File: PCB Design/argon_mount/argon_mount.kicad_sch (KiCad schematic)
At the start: 5 parts, among them CN2 1X4SMT, U1 MIC5219-2.85YM5, U2 VL6180

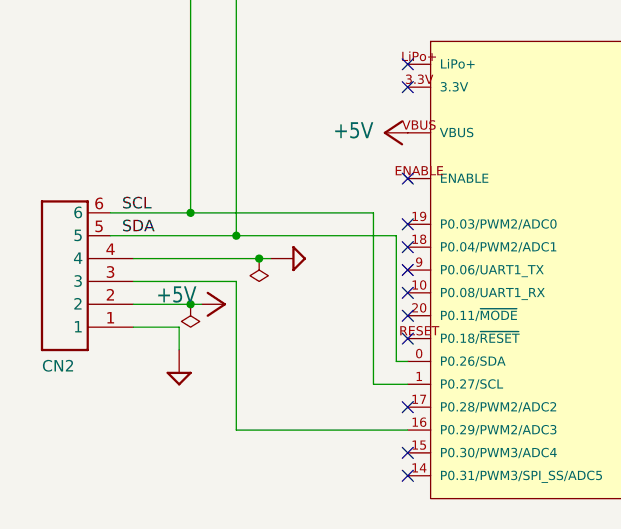
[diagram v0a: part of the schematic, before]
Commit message: argon pcb fix
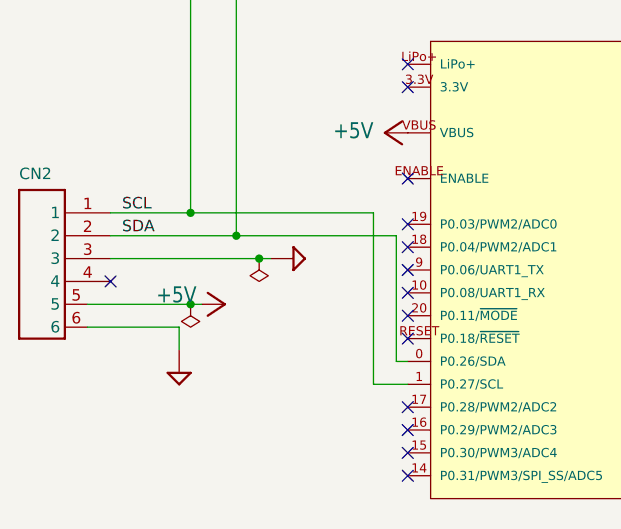
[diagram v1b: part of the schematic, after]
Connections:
- net +5V: now also CN2.5; no longer CN2.2
- net GND: now also CN2.3, CN2.6; no longer CN2.1, CN2.4
- net SCL: now also CN2.1; no longer CN2.6
- net SDA: now also CN2.2; no longer CN2.5
- net at MD1.16 (P0.29/PWM2/ADC3): no longer CN2.3
- no-connect marks 27 -> 29
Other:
- moved on the sheet: CN2
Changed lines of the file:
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@@
   (no_connect (at 71.12 120.65))
   (no_connect (at 71.12 66.04))
+  (no_connect (at 71.12 138.43))
   (no_connect (at 71.12 97.79))
   (no_connect (at 71.12 110.49))
   (no_connect (at 71.12 100.33))
+  (no_connect (at 38.1 121.92))
   (no_connect (at 71.12 115.57))
   (no_connect (at 71.12 118.11))
@@
   (no_connect (at 71.12 140.97))
   (no_connect (at 71.12 143.51))
-  (wire (pts (xy 52.07 138.43) (xy 52.07 121.92))
-    (stroke (width 0) (type default) (color 0 0 0 0))
-  )
   (wire (pts (xy 104.14 73.66) (xy 104.14 66.04))
     (stroke (width 0) (type default) (color 0 0 0 0))
   )
-  (wire (pts (xy 40.64 127) (xy 45.72 127))
+  (wire (pts (xy 35.56 127) (xy 45.72 127))
     (stroke (width 0) (type default) (color 0 0 0 0))
   )
@@
     (stroke (width 0) (type default) (color 0 0 0 0))
   )
-  (wire (pts (xy 40.64 124.46) (xy 46.99 124.46))
-    (stroke (width 0) (type default) (color 0 0 0 0))
-  )
-  (wire (pts (xy 40.64 119.38) (xy 54.61 119.38))
+  (wire (pts (xy 35.56 124.46) (xy 46.99 124.46))
+    (stroke (width 0) (type default) (color 0 0 0 0))
+  )
+  (wire (pts (xy 38.1 119.38) (xy 54.61 119.38))
     (stroke (width 0) (type default) (color 0 0 0 0))
   )
@@
     (stroke (width 0) (type default) (color 0 0 0 0))
   )
-  (wire (pts (xy 71.12 138.43) (xy 52.07 138.43))
-    (stroke (width 0) (type default) (color 0 0 0 0))
-  )
   (wire (pts (xy 101.6 73.66) (xy 104.14 73.66))
     (stroke (width 0) (type default) (color 0 0 0 0))
@@
   )
   (wire (pts (xy 72.39 35.56) (xy 72.39 38.1))
-    (stroke (width 0) (type default) (color 0 0 0 0))
-  )
-  (wire (pts (xy 52.07 121.92) (xy 40.64 121.92))
     (stroke (width 0) (type default) (color 0 0 0 0))
   )
@@
     (pin "1")
   )
-  (symbol (lib_id "Adafruit NeoPixel 8 Stick-eagle-import:1X4SMT") (at 35.56 124.46 180) (unit 1)
-    (in_bom yes) (on_board yes)
-    (property "Reference" "CN2" (id 0) (at 30.48 132.08 0)
+  (symbol (lib_id "Adafruit NeoPixel 8 Stick-eagle-import:1X4SMT") (at 33.02 116.84 0) (mirror y) (unit 1)
+    (in_bom yes) (on_board yes)
+    (property "Reference" "CN2" (id 0) (at 27.94 109.22 0)
       (effects (font (size 1.27 1.27)) (justify right top))
     )
-    (property "Value" "1X4SMT" (id 1) (at 35.56 114.3 0)
+    (property "Value" "1X4SMT" (id 1) (at 33.02 127 0)
       (effects (font (size 1.27 1.27)) (justify left bottom) hide)
     )
-    (property "Footprint" "Adafruit NeoPixel 8 Stick:1X4-SMT" (id 2) (at 35.56 124.46 0)
-      (effects (font (size 1.27 1.27)) hide)
-    )
-    (property "Datasheet" "" (id 3) (at 35.56 124.46 0)
-      (effects (font (size 1.27 1.27)) hide)
-    )
+    (property "Footprint" "Adafruit NeoPixel 8 Stick:1X4-SMT" (id 2) (at 33.02 116.84 0)
+      (effects (font (size 1.27 1.27)) hide)
+    )
+    (property "Datasheet" "" (id 3) (at 33.02 116.84 0)
+      (effects (font (size 1.27 1.27)) hide)
+    )
